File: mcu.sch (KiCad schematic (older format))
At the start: 44 parts

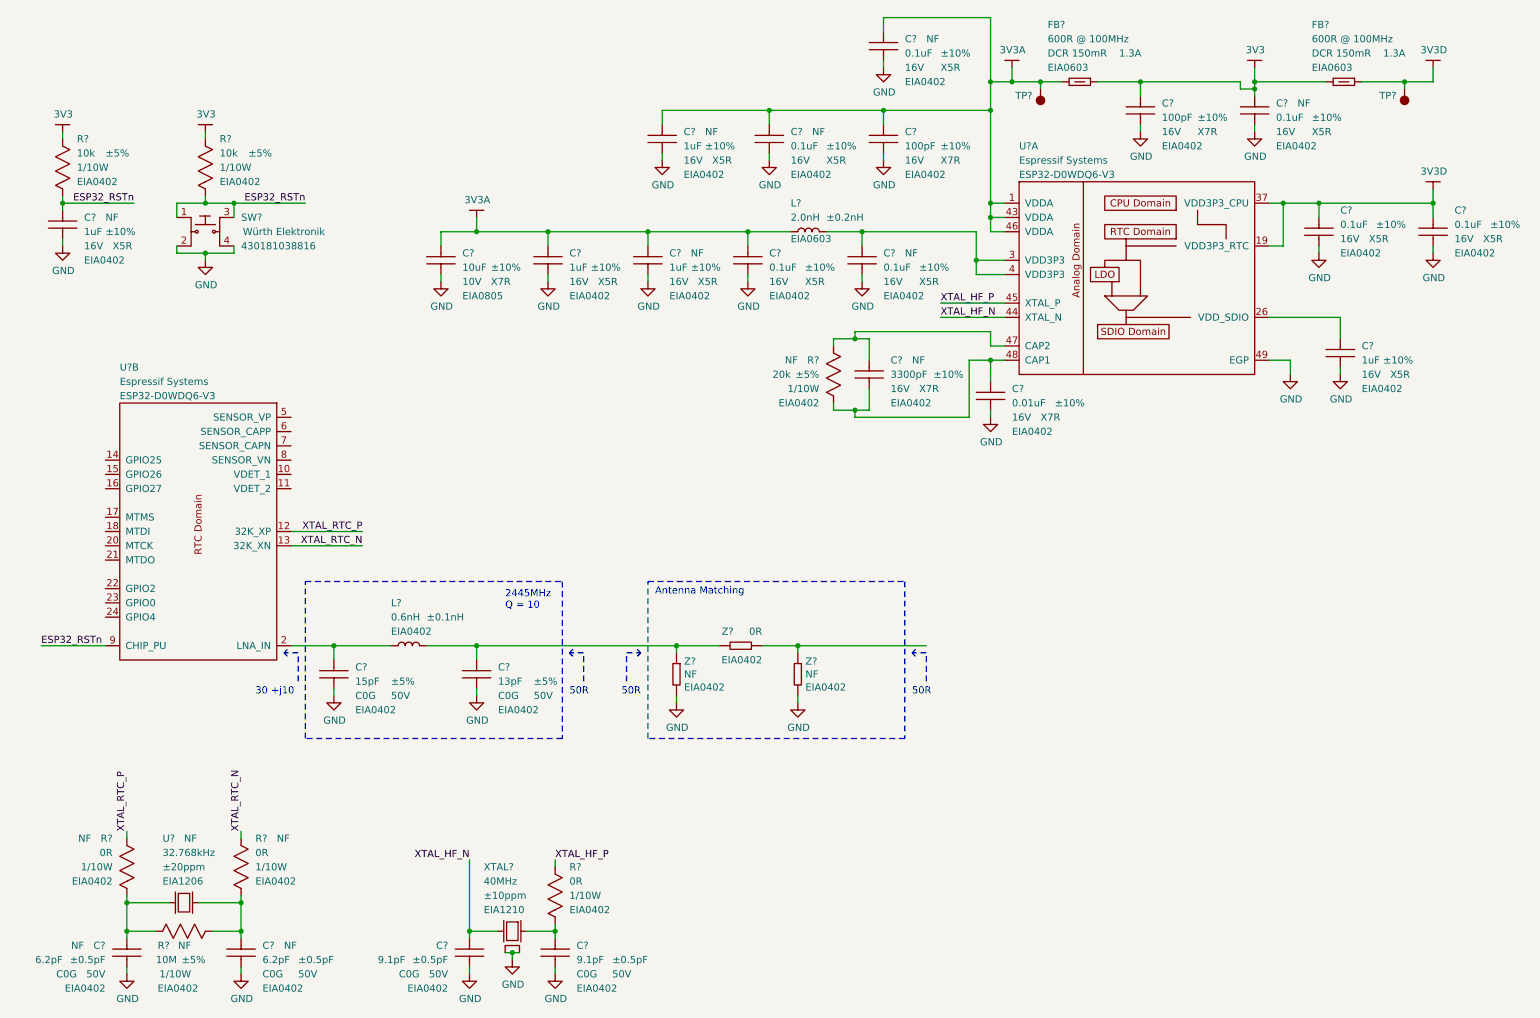
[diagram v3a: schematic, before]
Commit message: Add BOOT_MODE tact switch.
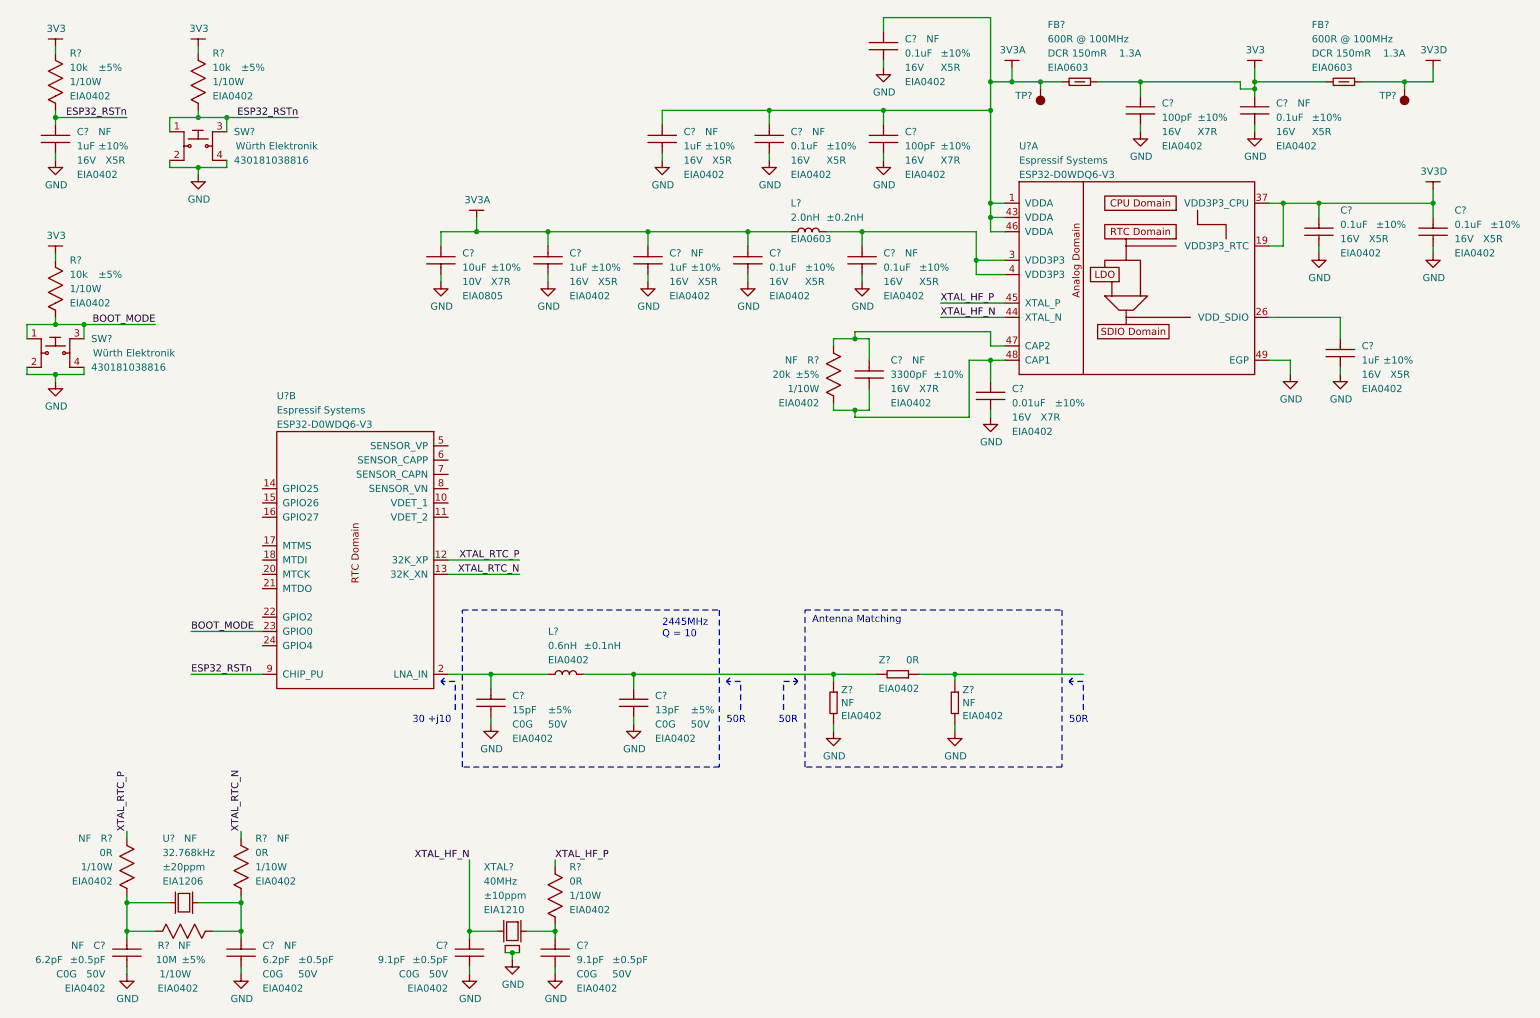
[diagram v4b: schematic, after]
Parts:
- added R?: RES-EIA0402, footprints_generic:RESC100X50X40L25NN, symbol gz_Chip-Resistors-Surface-Mount:RES-EIA0402
- added SW?: WE-430181038816, footprints:WE-430181038816_SWSOFL4P150_450X750X380L150X70N, symbol gz_Tactile-Switches:WE-430181038816
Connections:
- net +3V3: now also R?.1
- net GND: now also SW?.2, SW?.4
- net BOOT_MODE: now reaches U?.23 (GPIO0)
- net BOOT_MODE: now also R?.2, SW?.1, SW?.3
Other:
- moved on the sheet: C?, L?, R?, SW?, U?B, Z?

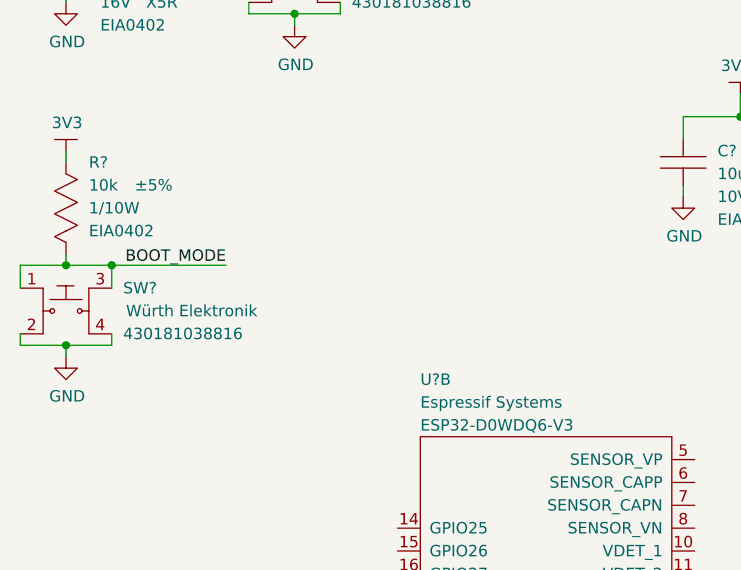
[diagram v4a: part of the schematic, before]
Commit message: Add power and boot mode LED's.
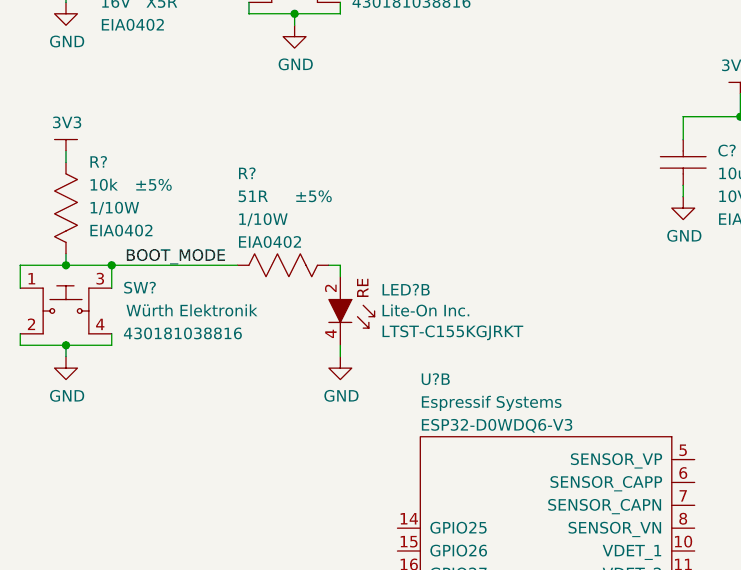
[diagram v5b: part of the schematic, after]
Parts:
- added LED?: LiteOn-LTST-C155KGJRKT, footprints:LiteOn-LTST-C155_LEDCAV4P138_270X320X110L50X90N, symbol gz_LED-Indication-Discrete:LiteOn-LTST-C155KGJRKT
- added R?: RES-EIA0402, footprints_generic:RESC100X50X40L25NN, symbol gz_Chip-Resistors-Surface-Mount:RES-EIA0402
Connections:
- net BOOT_MODE: now also R?.1
- net GND: now also LED?.4 (C)
- new net: LED?.2 (A), R?.2
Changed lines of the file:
@@
 	850  3150 1050 3150
 Connection ~ 1050 2800
-Wire Wire Line
-	1050 2800 1550 2800
 Text Label 1550 2800 2    50   ~ 0
 BOOT_MODE
+$Comp
+L gz_LED-Indication-Discrete:LiteOn-LTST-C155KGJRKT LED?
+U 2 1 604FF3FC
+P 2050 2950
+AR Path="/6032FC47/604FF3FC" Ref="LED?"  Part="2"
+AR Path="/60330427/604FF3FC" Ref="LED?"  Part="2"
+F 0 "LED?" V 2009 3128 50  0000 L CNN
+F 1 "LiteOn-LTST-C155KGJRKT" H 2600 4200 50  0001 L CNN
+F 2 "footprints:LiteOn-LTST-C155_LEDCAV4P138_270X320X110L50X90N" H 2600 4100 50  0001 L CNN
+F 3 "http://optoelectronics.liteon.com/upload/download/DS22-2001-038/LTST-C155KGJRKT.pdf" H 1150 3650 50  0001 L CNN
+F 4 "Digikey" H 2600 4000 50  0001 L CNN "Vendor"
+F 5 "160-1409-1-ND" H 3000 4000 50  0001 L CNN "Vendor_PN"
+F 6 "Lite-On Inc." V 2100 3128 50  0000 L CNN "Manufacturer"
+F 7 "LTST-C155KGJRKT" V 2191 3128 50  0000 L CNN "MPN"
+F 8 "Optoelectronics" H 2600 3900 50  0001 L CNN "Category"
+F 9 "LED Indication - Discrete" H 2600 3800 50  0001 L CNN "Family"
+F 10 "Yes" H 2050 3500 50  0001 L CNN "Fit"
+	2    2050 2950
+	0    1    1    0
+$EndComp
+$Comp
+L gz_Chip-Resistors-Surface-Mount:RES-EIA0402 R?
+U 1 1 6051C6B0
+P 1800 2800
+AR Path="/6032FC47/6051C6B0" Ref="R?"  Part="1"
+AR Path="/60330427/6051C6B0" Ref="R?"  Part="1"
+F 0 "R?" H 1600 3200 50  0000 L CNN
+F 1 "RES-EIA0402" H 2600 3700 50  0001 L CNN
+F 2 "footprints_generic:RESC100X50X40L25NN" H -1500 7150 50  0001 L CNN
+F 3 "${PANASONIC_GP_CHIP_RES_BASE}ERJ2GEJ510X" H -1500 7250 50  0001 L CNN
+F 4 "Digikey" H 1800 2800 50  0001 L CNN "Vendor"
+F 5 "P51JCT-ND" H 1800 2800 50  0001 L CNN "Vendor_PN"
+F 6 "Panasonic Electronic Components" H 2600 3500 50  0001 L CNN "Manufacturer"
+F 7 "ERJ2GEJ510X" H 2600 3400 50  0001 L CNN "MPN"
+F 8 "Resistors" H -1500 7550 50  0001 L CNN "Category"
+F 9 "Chip Resistor - Surface Mount" H -1500 7650 50  0001 L CNN "Family"
+F 10 "Yes" H 1800 2800 50  0001 L CNN "Fit"
+F 11 "51R" H 1600 3100 50  0000 L CNN "Resistance"
+F 12 "±5%" H 1850 3100 50  0000 L CNN "Tolerance"
+F 13 "1/10W" H 1600 3000 50  0000 L CNN "Power"
+F 14 "N/A" V 1936 2878 50  0001 L CNN "Voltage"
+F 15 "EIA0402" H 1600 2900 50  0000 L CNN "Package"
+	1    1800 2800
+	1    0    0    -1
+$EndComp
+$Comp
+L gz_Power-Symbols:GND #PWR?
+U 1 1 6052D922
+P 2050 3200
+AR Path="/60330427/6052D922" Ref="#PWR?"  Part="1"
+AR Path="/606CDE66/6052D922" Ref="#PWR?"  Part="1"
+F 0 "#PWR?" H 2050 2950 50  0001 C CNN
+F 1 "GND" H 2055 3027 50  0000 C CNN
+F 2 "" H 2050 3200 50  0001 C CNN
+F 3 "" H 2050 3200 50  0001 C CNN
+	1    2050 3200
+	1    0    0    -1
+$EndComp
+Wire Wire Line
+	2050 3150 2050 3200
+Wire Wire Line
+	2050 2850 2050 2800
+Wire Wire Line
+	2000 2800 2050 2800
+Wire Wire Line
+	1050 2800 1600 2800
 $EndSCHEMATC

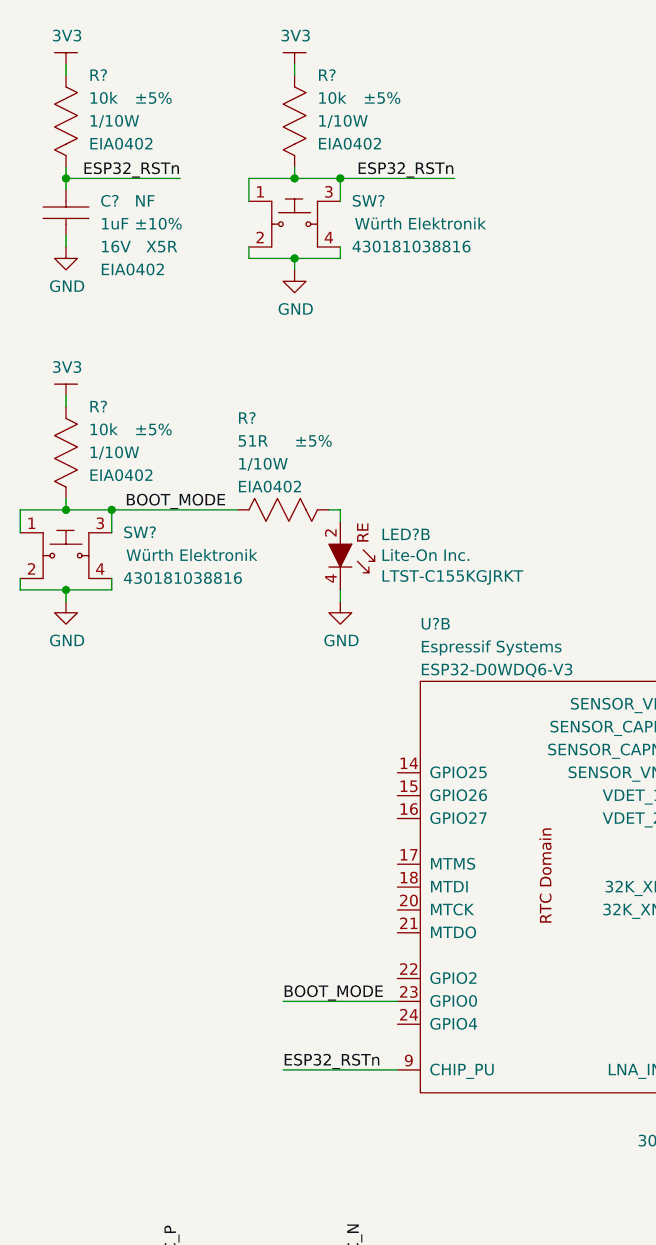
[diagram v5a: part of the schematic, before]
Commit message: Add auto-flash circuit to prevent DTR == 1 && RTS == 1 condition to keep ESP32 in reset.
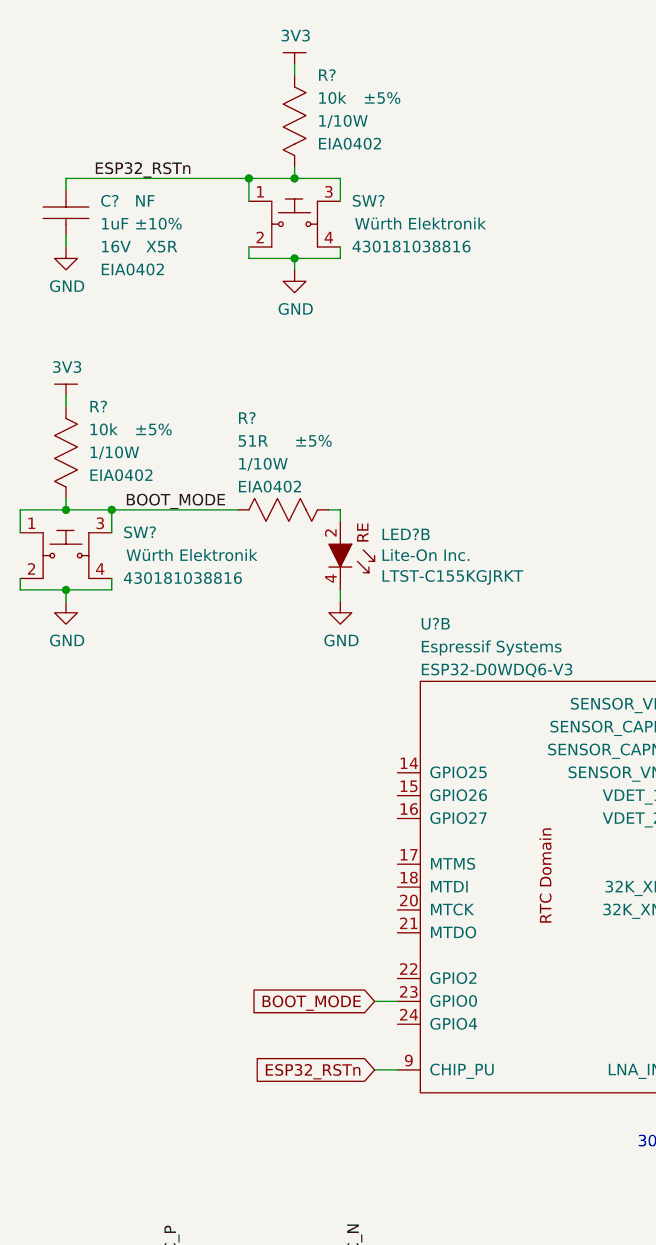
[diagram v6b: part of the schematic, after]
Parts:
- removed R?: RES-EIA0402, footprints_generic:RESC100X50X40L25NN, symbol gz_Chip-Resistors-Surface-Mount:RES-EIA0402
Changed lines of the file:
@@
 $EndComp
 Wire Wire Line
-	2300 5250 1800 5250
-Text Label 1800 5250 0    50   ~ 0
-ESP32_RSTn
+	2300 5250 2200 5250
 Text Label 4100 4550 2    50   ~ 0
 XTAL_RTC_N
@@
 Antenna Matching\n
 $Comp
-L gz_Chip-Resistors-Surface-Mount:RES-EIA0402 R?
-U 1 1 60760D91
-P 850 1100
-AR Path="/60330427/60760D91" Ref="R?"  Part="1"
-AR Path="/606CDE66/60760D91" Ref="R?"  Part="1"
-F 0 "R?" V 650 1200 50  0000 L CNN
-F 1 "RES-EIA0402" H 1650 2000 50  0001 L CNN
-F 2 "footprints_generic:RESC100X50X40L25NN" H -2450 5450 50  0001 L CNN
-F 3 "${PANASONIC_GP_CHIP_RES_BASE}ERJ2GEJ103X" H -2450 5550 50  0001 L CNN
-F 4 "Digikey" H 850 1100 50  0001 L CNN "Vendor"
-F 5 "P10KJCT-ND" H 850 1100 50  0001 L CNN "Vendor_PN"
-F 6 "Panasonic Electronic Components" H 1650 1800 50  0001 L CNN "Manufacturer"
-F 7 "ERJ2GEJ103X" H 1650 1700 50  0001 L CNN "MPN"
-F 8 "Resistors" H -2450 5850 50  0001 L CNN "Category"
-F 9 "Chip Resistor - Surface Mount" H -2450 5950 50  0001 L CNN "Family"
-F 10 "Yes" H 850 1100 50  0001 C CNN "Fit"
-F 11 "10k" V 750 1200 50  0000 L CNN "Resistance"
-F 12 "±5%" V 750 1400 50  0000 L CNN "Tolerance"
-F 13 "1/10W" V 850 1200 50  0000 L CNN "Power"
-F 14 "N/A" H 850 1315 50  0001 L CNN "Voltage"
-F 15 "EIA0402" V 950 1200 50  0000 L CNN "Package"
-	1    850  1100
-	0    1    1    0
-$EndComp
-$Comp
 L gz_Ceramic-Capacitors:CAP-EIA0402 C?
 U 1 1 60760DA3
@@
 	1    0    0    -1
 $EndComp
-$Comp
-L gz_Power-Symbols:3V3 #PWR?
-U 1 1 60760DAF
-P 850 850
-AR Path="/60330427/60760DAF" Ref="#PWR?"  Part="1"
-AR Path="/606CDE66/60760DAF" Ref="#PWR?"  Part="1"
-F 0 "#PWR?" H 1000 800 50  0001 C CNN
-F 1 "3V3" H 855 973 50  0000 C CNN
-F 2 "" H 850 850 50  0001 C CNN
-F 3 "" H 850 850 50  0001 C CNN
-	1    850  850
-	1    0    0    -1
-$EndComp
-Wire Wire Line
-	850  850  850  900
-Wire Wire Line
-	850  1300 850  1350
 Wire Wire Line
 	850  1600 850  1650
-Connection ~ 850  1350
 Wire Wire Line
 	850  1350 850  1400
-Text Label 1350 1350 2    50   ~ 0
-ESP32_RSTn
-Wire Wire Line
-	850  1350 1350 1350
 $Comp
 L gz_Tactile-Switches:WE-430181038816 SW?
@@
 Wire Wire Line
 	2050 1350 2050 1450
-Text Label 2550 1350 2    50   ~ 0
+Text Label 1400 1350 2    50   ~ 0
 ESP32_RSTn
 Wire Wire Line
@@
 Wire Wire Line
 	1850 1700 2050 1700
-Connection ~ 2050 1350
-Wire Wire Line
-	2050 1350 2550 1350
-Wire Wire Line
-	2300 4950 1800 4950
-Text Label 1800 4950 0    50   ~ 0
-BOOT_MODE
+Wire Wire Line
+	2300 4950 2200 4950
 $Comp
 L gz_Tactile-Switches:WE-430181038816 SW?
@@
 Wire Wire Line
 	1050 2800 1600 2800
+Text GLabel 2200 5250 0    50   Input ~ 0
+ESP32_RSTn
+Text GLabel 2200 4950 0    50   Input ~ 0
+BOOT_MODE
+Wire Wire Line
+	850  1350 1650 1350
+Connection ~ 1650 1350
 $EndSCHEMATC

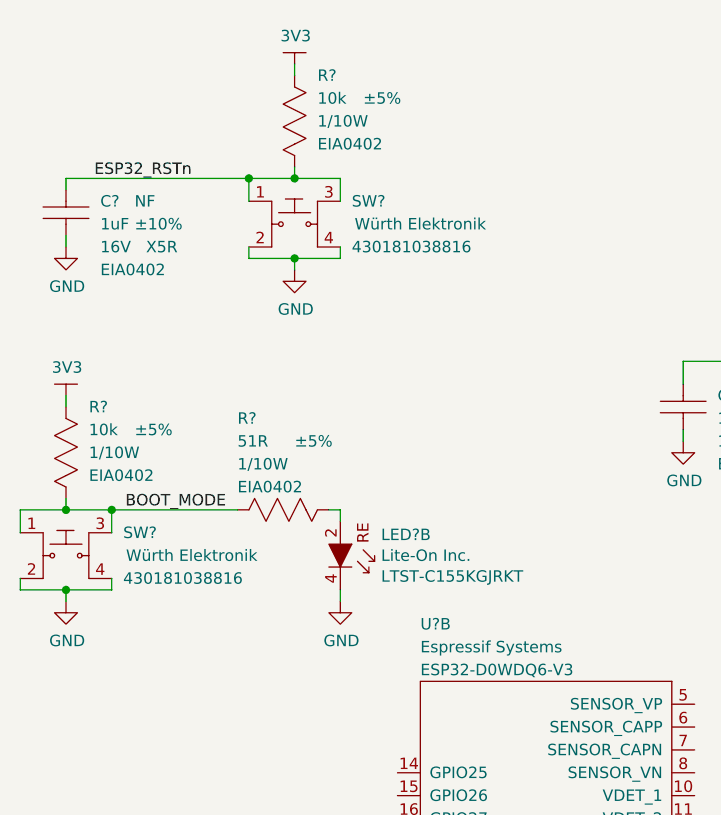
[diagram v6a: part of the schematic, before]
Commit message: Fix Boot Mode LED circuit (add PNP drive); add 2x BiColour general-purpose LED's.
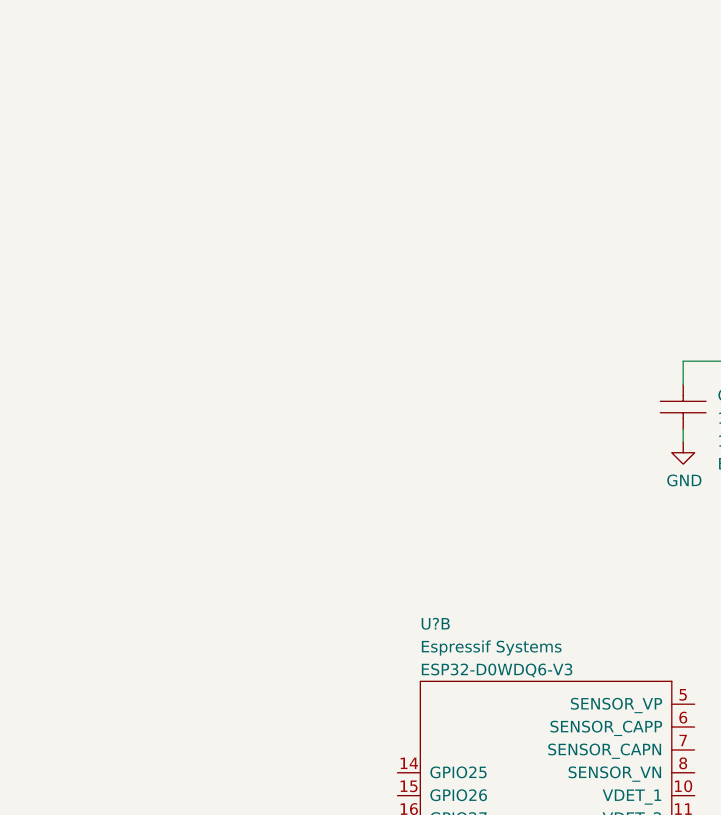
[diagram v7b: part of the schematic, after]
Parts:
- removed C?: CAP-EIA0402, footprints_generic:CAPC100X50X55L30N, symbol gz_Ceramic-Capacitors:CAP-EIA0402
- removed LED?: LiteOn-LTST-C155KGJRKT, footprints:LiteOn-LTST-C155_LEDCAV4P138_270X320X110L50X90N, symbol gz_LED-Indication-Discrete:LiteOn-LTST-C155KGJRKT
- removed R? (x3): RES-EIA0402, footprints_generic:RESC100X50X40L25NN, symbol gz_Chip-Resistors-Surface-Mount:RES-EIA0402
- removed SW? (x2): WE-430181038816, footprints:WE-430181038816_SWSOFL4P150_450X750X380L150X70N, symbol gz_Tactile-Switches:WE-430181038816
